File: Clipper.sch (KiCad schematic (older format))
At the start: 38 parts

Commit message: First complete system.  Still a few things to check.
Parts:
- removed C? (x3): C, ~, symbol C
- removed R? (x7): 4.7k, ~, symbol R
- added C? (x3): 470n, ~, symbol C
- added R? (x7): 1k, ~, symbol R
- C?: value C -> 470n; Type (none) -> Ceramic
- R?: value 4.7k -> 1k
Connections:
- net +15V: now also C?.1
- net -15V: now also C?.2, C?.2
- net AGND: now also C?.1, C?.1, C?.2
- net LIN: now also R?.1
- net RIN: now also R?.1
- net ROUT: now also R?.2
- net at D?.2 (K), R?.1: now also R?.1 (x4)
- net at R?.1, U?.6 (_): now also R?.2, R?.2, R?.2
- net at U?.6 (_): now also R?.1, R?.2, R?.2, R?.2
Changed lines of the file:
@@
 LIBS:my-conn
 LIBS:ADC-cache
-EELAYER 24 0
+EELAYER 27 0
 EELAYER END
 $Descr A4 11693 8268
@@
 Sheet 5 6
 Title ""
-Date "12 may 2014"
+Date "21 may 2014"
 Rev ""
 Comp ""
@@
 $Comp
 L R R?
-U 1 1 536E7363
-P 3600 3400
-F 0 "R?" V 3680 3400 40  0000 C CNN
-F 1 "4.7k" V 3607 3401 40  0000 C CNN
-F 2 "~" V 3530 3400 30  0000 C CNN
-F 3 "~" H 3600 3400 30  0000 C CNN
-	1    3600 3400
-	0    -1   -1   0
-$EndComp
-$Comp
-L R R?
-U 1 1 536E73C0
-P 3600 3700
-F 0 "R?" V 3680 3700 40  0000 C CNN
-F 1 "4.7k" V 3607 3701 40  0000 C CNN
-F 2 "~" V 3530 3700 30  0000 C CNN
-F 3 "~" H 3600 3700 30  0000 C CNN
-	1    3600 3700
-	0    -1   -1   0
-$EndComp
-$Comp
-L R R?
-U 1 1 536E742F
-P 3600 4000
-F 0 "R?" V 3680 4000 40  0000 C CNN
-F 1 "4.7k" V 3607 4001 40  0000 C CNN
-F 2 "~" V 3530 4000 30  0000 C CNN
-F 3 "~" H 3600 4000 30  0000 C CNN
-	1    3600 4000
-	0    -1   -1   0
-$EndComp
-$Comp
-L R R?
 U 1 1 536E799F
 P 1450 4950
@@
 P 4750 3200
 F 0 "R?" V 4830 3200 40  0000 C CNN
-F 1 "4.7k" V 4757 3201 40  0000 C CNN
+F 1 "1k" V 4757 3201 40  0000 C CNN
 F 2 "~" V 4680 3200 30  0000 C CNN
 F 3 "~" H 4750 3200 30  0000 C CNN
@@
 $Comp
 L R R?
-U 1 1 536E837F
-P 9000 3400
-F 0 "R?" V 9080 3400 40  0000 C CNN
-F 1 "4.7k" V 9007 3401 40  0000 C CNN
-F 2 "~" V 8930 3400 30  0000 C CNN
-F 3 "~" H 9000 3400 30  0000 C CNN
-	1    9000 3400
-	0    -1   -1   0
-$EndComp
-$Comp
-L R R?
-U 1 1 536E8385
-P 9000 3700
-F 0 "R?" V 9080 3700 40  0000 C CNN
-F 1 "4.7k" V 9007 3701 40  0000 C CNN
-F 2 "~" V 8930 3700 30  0000 C CNN
-F 3 "~" H 9000 3700 30  0000 C CNN
-	1    9000 3700
-	0    -1   -1   0
-$EndComp
-$Comp
-L R R?
-U 1 1 536E838B
-P 9000 4000
-F 0 "R?" V 9080 4000 40  0000 C CNN
-F 1 "4.7k" V 9007 4001 40  0000 C CNN
-F 2 "~" V 8930 4000 30  0000 C CNN
-F 3 "~" H 9000 4000 30  0000 C CNN
-	1    9000 4000
-	0    -1   -1   0
-$EndComp
-$Comp
-L R R?
 U 1 1 536E8391
 P 6850 4950
@@
 Text HLabel 9550 4000 3    60   Input ~ 0
 AGND
-$Comp
-L R R?
-U 1 1 536E83F0
-P 10150 3200
-F 0 "R?" V 10230 3200 40  0000 C CNN
-F 1 "4.7k" V 10157 3201 40  0000 C CNN
-F 2 "~" V 10080 3200 30  0000 C CNN
-F 3 "~" H 10150 3200 30  0000 C CNN
-	1    10150 3200
-	0    -1   -1   0
-$EndComp
 Text HLabel 10050 3400 0    60   Input ~ 0
 +15V
@@
 P 5450 1700
 F 0 "C?" H 5450 1800 40  0000 L CNN
-F 1 "C" H 5456 1615 40  0000 L CNN
+F 1 "470n" H 5456 1615 40  0000 L CNN
 F 2 "~" H 5488 1550 30  0000 C CNN
 F 3 "~" H 5450 1700 60  0000 C CNN
+F 4 "Ceramic" H 5450 1700 60  0001 C CNN "Type"
 	1    5450 1700
-	1    0    0    -1
-$EndComp
-$Comp
-L C C?
-U 1 1 536EC1ED
-P 5800 1700
-F 0 "C?" H 5800 1800 40  0000 L CNN
-F 1 "C" H 5806 1615 40  0000 L CNN
-F 2 "~" H 5838 1550 30  0000 C CNN
-F 3 "~" H 5800 1700 60  0000 C CNN
-	1    5800 1700
 	1    0    0    -1
 $EndComp
@@
 Text HLabel 5250 1900 0    60   Input ~ 0
 AGND
-$Comp
-L C C?
-U 1 1 536EC4B0
-P 5450 2100
-F 0 "C?" H 5450 2200 40  0000 L CNN
-F 1 "C" H 5456 2015 40  0000 L CNN
-F 2 "~" H 5488 1950 30  0000 C CNN
-F 3 "~" H 5450 2100 60  0000 C CNN
-	1    5450 2100
-	1    0    0    -1
-$EndComp
-$Comp
-L C C?
-U 1 1 536EC4B6
-P 5800 2100
-F 0 "C?" H 5800 2200 40  0000 L CNN
-F 1 "C" H 5806 2015 40  0000 L CNN
-F 2 "~" H 5838 1950 30  0000 C CNN
-F 3 "~" H 5800 2100 60  0000 C CNN
-	1    5800 2100
-	1    0    0    -1
-$EndComp
 Wire Wire Line
 	1850 2850 1850 3050
@@
 Wire Wire Line
 	5250 1900 5800 1900
+$Comp
+L C C?
+U 1 1 537C3D88
+P 5800 1700
+F 0 "C?" H 5800 1800 40  0000 L CNN
+F 1 "470n" H 5806 1615 40  0000 L CNN
+F 2 "~" H 5838 1550 30  0000 C CNN
+F 3 "~" H 5800 1700 60  0000 C CNN
+F 4 "Ceramic" H 5800 1700 60  0001 C CNN "Type"
+	1    5800 1700
+	1    0    0    -1
+$EndComp
+$Comp
+L C C?
+U 1 1 537C3D8F
+P 5450 2100
+F 0 "C?" H 5450 2200 40  0000 L CNN
+F 1 "470n" H 5456 2015 40  0000 L CNN
+F 2 "~" H 5488 1950 30  0000 C CNN
+F 3 "~" H 5450 2100 60  0000 C CNN
+F 4 "Ceramic" H 5450 2100 60  0001 C CNN "Type"
+	1    5450 2100
+	1    0    0    -1
+$EndComp
+$Comp
+L C C?
+U 1 1 537C3D96
+P 5800 2100
+F 0 "C?" H 5800 2200 40  0000 L CNN
+F 1 "470n" H 5806 2015 40  0000 L CNN
+F 2 "~" H 5838 1950 30  0000 C CNN
+F 3 "~" H 5800 2100 60  0000 C CNN
+F 4 "Ceramic" H 5800 2100 60  0001 C CNN "Type"
+	1    5800 2100
+	1    0    0    -1
+$EndComp
+$Comp
+L R R?
+U 1 1 537C500E
+P 3600 3400
+F 0 "R?" V 3680 3400 40  0000 C CNN
+F 1 "1k" V 3607 3401 40  0000 C CNN
+F 2 "~" V 3530 3400 30  0000 C CNN
+F 3 "~" H 3600 3400 30  0000 C CNN
+	1    3600 3400
+	0    -1   -1   0
+$EndComp
+$Comp
+L R R?
+U 1 1 537C5014
+P 3600 3700
+F 0 "R?" V 3680 3700 40  0000 C CNN
+F 1 "1k" V 3607 3701 40  0000 C CNN
+F 2 "~" V 3530 3700 30  0000 C CNN
+F 3 "~" H 3600 3700 30  0000 C CNN
+	1    3600 3700
+	0    -1   -1   0
+$EndComp
+$Comp
+L R R?
+U 1 1 537C501A
+P 3600 4000
+F 0 "R?" V 3680 4000 40  0000 C CNN
+F 1 "1k" V 3607 4001 40  0000 C CNN
+F 2 "~" V 3530 4000 30  0000 C CNN
+F 3 "~" H 3600 4000 30  0000 C CNN
+	1    3600 4000
+	0    -1   -1   0
+$EndComp
+$Comp
+L R R?
+U 1 1 537C5020
+P 9000 3400
+F 0 "R?" V 9080 3400 40  0000 C CNN
+F 1 "1k" V 9007 3401 40  0000 C CNN
+F 2 "~" V 8930 3400 30  0000 C CNN
+F 3 "~" H 9000 3400 30  0000 C CNN
+	1    9000 3400
+	0    -1   -1   0
+$EndComp
+$Comp
+L R R?
+U 1 1 537C5026
+P 9000 3700
+F 0 "R?" V 9080 3700 40  0000 C CNN
+F 1 "1k" V 9007 3701 40  0000 C CNN
+F 2 "~" V 8930 3700 30  0000 C CNN
+F 3 "~" H 9000 3700 30  0000 C CNN
+	1    9000 3700
+	0    -1   -1   0
+$EndComp
+$Comp
+L R R?
+U 1 1 537C502C
+P 9000 4000
+F 0 "R?" V 9080 4000 40  0000 C CNN
+F 1 "1k" V 9007 4001 40  0000 C CNN
+F 2 "~" V 8930 4000 30  0000 C CNN
+F 3 "~" H 9000 4000 30  0000 C CNN
+	1    9000 4000
+	0    -1   -1   0
+$EndComp
+$Comp
+L R R?
+U 1 1 537C5032
+P 10150 3200
+F 0 "R?" V 10230 3200 40  0000 C CNN
+F 1 "1k" V 10157 3201 40  0000 C CNN
+F 2 "~" V 10080 3200 30  0000 C CNN
+F 3 "~" H 10150 3200 30  0000 C CNN
+	1    10150 3200
+	0    -1   -1   0
+$EndComp
 $EndSCHEMATC

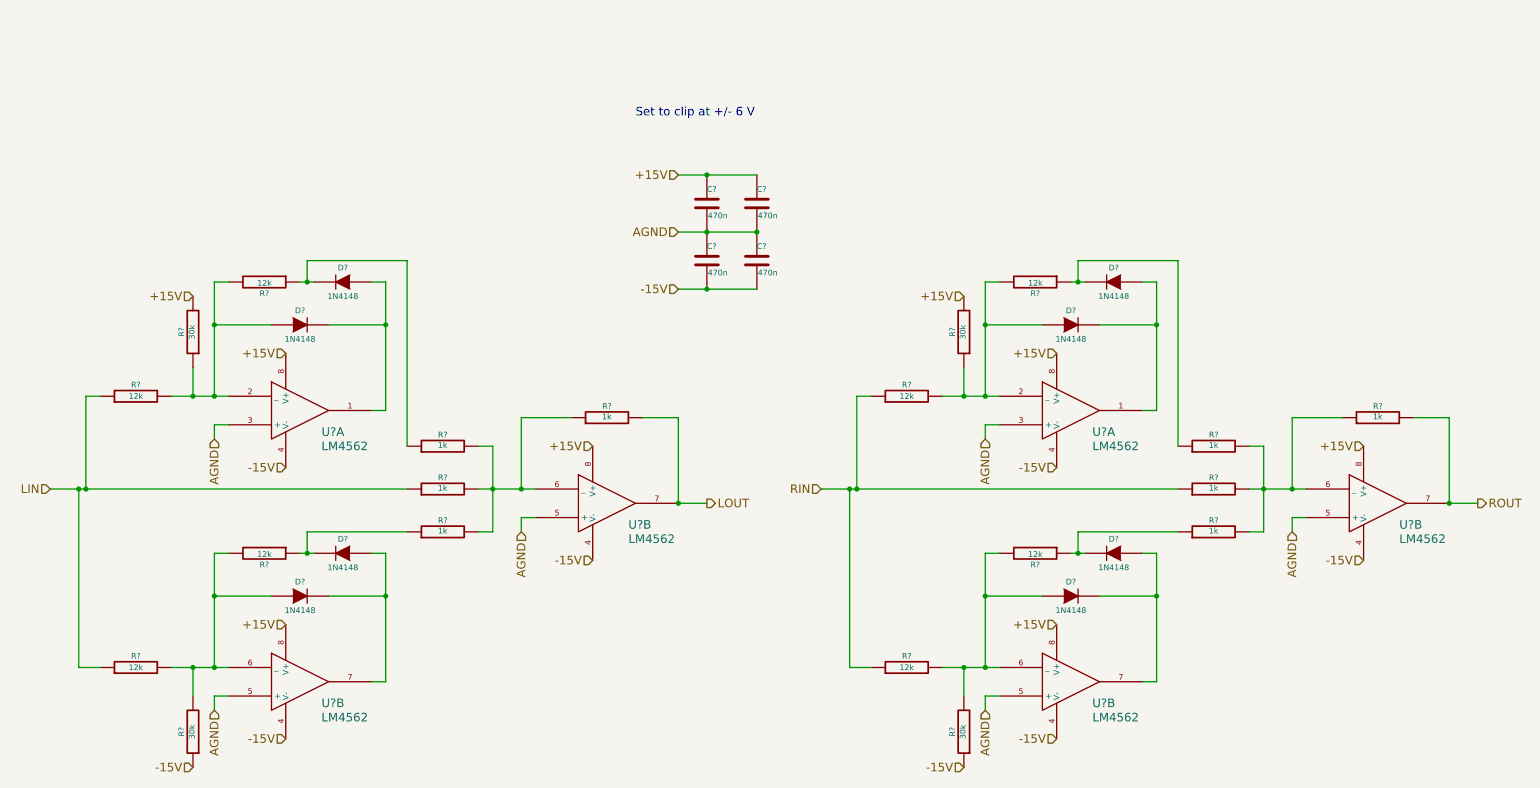
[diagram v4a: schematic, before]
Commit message: Noise analysis completed; signal section finished.
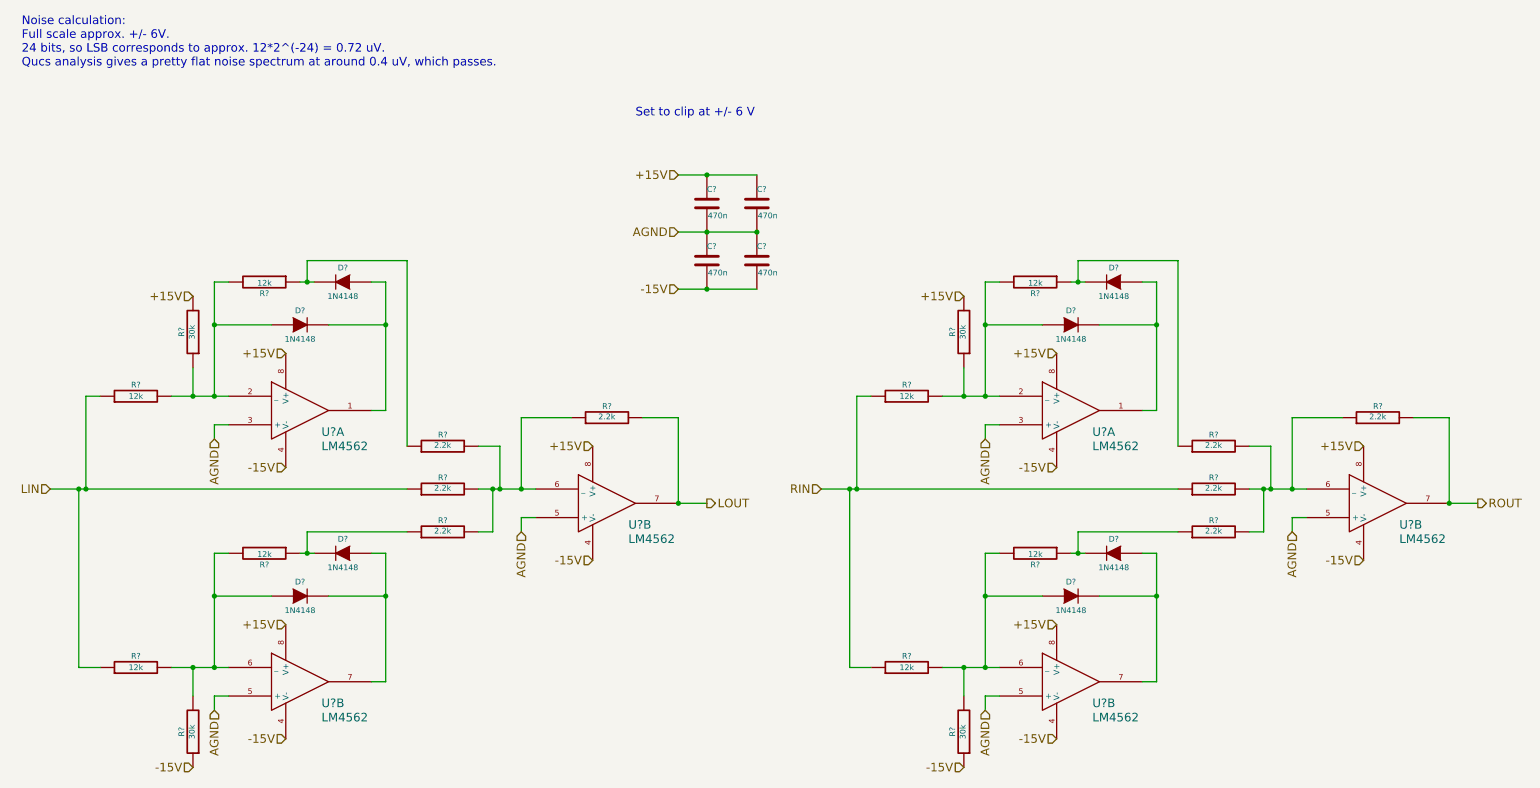
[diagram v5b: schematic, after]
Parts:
- removed R? (x7): 1k, ~, symbol R
- added R? (x7): 2.2k, ~, symbol R
- R?: value 1k -> 2.2k
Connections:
- net LIN: now also R?.1
- net LOUT: now also R?.2
- net RIN: now also R?.1
- net ROUT: now also R?.2
- net at D?.2 (K), R?.1: now also R?.1 (x3)
- net at R?.2, U?.6 (_): now also R?.1, R?.2, R?.2
- net at U?.6 (_): now also R?.1, R?.2, R?.2, R?.2
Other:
- note added: "Noise calculation:\nFull scale approx. +/- 6V.\n24 bits, so LSB corresponds to approx. 12*2^(-24) = 0.72 uV.\nQucs analysis gives a pretty flat noise spectrum at around 0.4 uV, which passes."
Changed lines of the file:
@@
 Text HLabel 4150 4000 3    60   Input ~ 0
 AGND
-$Comp
-L R R?
-U 1 1 536E7BF7
-P 4750 3200
-F 0 "R?" V 4830 3200 40  0000 C CNN
-F 1 "1k" V 4757 3201 40  0000 C CNN
-F 2 "~" V 4680 3200 30  0000 C CNN
-F 3 "~" H 4750 3200 30  0000 C CNN
-	1    4750 3200
-	0    -1   -1   0
-$EndComp
 Text HLabel 4650 3400 0    60   Input ~ 0
 +15V
@@
 	3350 2100 2650 2100
 Wire Wire Line
-	3850 3400 3950 3400
-Wire Wire Line
-	3950 3400 3950 4000
+	3850 3400 4000 3400
 Connection ~ 1100 3700
 Wire Wire Line
@@
 	8750 2100 8050 2100
 Wire Wire Line
-	9250 3400 9350 3400
-Wire Wire Line
-	9350 3400 9350 4000
+	9250 3400 9400 3400
 Connection ~ 6500 3700
 Wire Wire Line
@@
 P 3600 3400
 F 0 "R?" V 3680 3400 40  0000 C CNN
-F 1 "1k" V 3607 3401 40  0000 C CNN
+F 1 "2.2k" V 3607 3401 40  0000 C CNN
 F 2 "~" V 3530 3400 30  0000 C CNN
 F 3 "~" H 3600 3400 30  0000 C CNN
@@
 	0    -1   -1   0
 $EndComp
-$Comp
-L R R?
-U 1 1 537C5014
+Wire Wire Line
+	4000 3400 4000 3700
+Connection ~ 4000 3700
+Wire Wire Line
+	3950 3700 3950 4000
+Wire Wire Line
+	9400 3400 9400 3700
+Connection ~ 9400 3700
+Wire Wire Line
+	9350 3700 9350 4000
+Text Notes 650  750  0    60   ~ 0
+Noise calculation:\nFull scale approx. +/- 6V.\n24 bits, so LSB corresponds to approx. 12*2^(-24) = 0.72 uV.\nQucs analysis gives a pretty flat noise spectrum at around 0.4 uV, which passes.
+$Comp
+L R R?
+U 1 1 537CA2E9
 P 3600 3700
 F 0 "R?" V 3680 3700 40  0000 C CNN
-F 1 "1k" V 3607 3701 40  0000 C CNN
+F 1 "2.2k" V 3607 3701 40  0000 C CNN
 F 2 "~" V 3530 3700 30  0000 C CNN
 F 3 "~" H 3600 3700 30  0000 C CNN
@@
 $Comp
 L R R?
-U 1 1 537C501A
+U 1 1 537CA2EF
 P 3600 4000
 F 0 "R?" V 3680 4000 40  0000 C CNN
-F 1 "1k" V 3607 4001 40  0000 C CNN
+F 1 "2.2k" V 3607 4001 40  0000 C CNN
 F 2 "~" V 3530 4000 30  0000 C CNN
 F 3 "~" H 3600 4000 30  0000 C CNN
@@
 $Comp
 L R R?
-U 1 1 537C5020
+U 1 1 537CA2F5
+P 4750 3200
+F 0 "R?" V 4830 3200 40  0000 C CNN
+F 1 "2.2k" V 4757 3201 40  0000 C CNN
+F 2 "~" V 4680 3200 30  0000 C CNN
+F 3 "~" H 4750 3200 30  0000 C CNN
+	1    4750 3200
+	0    -1   -1   0
+$EndComp
+$Comp
+L R R?
+U 1 1 537CA2FB
 P 9000 3400
 F 0 "R?" V 9080 3400 40  0000 C CNN
-F 1 "1k" V 9007 3401 40  0000 C CNN
+F 1 "2.2k" V 9007 3401 40  0000 C CNN
 F 2 "~" V 8930 3400 30  0000 C CNN
 F 3 "~" H 9000 3400 30  0000 C CNN
@@
 $Comp
 L R R?
-U 1 1 537C5026
+U 1 1 537CA301
 P 9000 3700
 F 0 "R?" V 9080 3700 40  0000 C CNN
-F 1 "1k" V 9007 3701 40  0000 C CNN
+F 1 "2.2k" V 9007 3701 40  0000 C CNN
 F 2 "~" V 8930 3700 30  0000 C CNN
 F 3 "~" H 9000 3700 30  0000 C CNN
@@
 $Comp
 L R R?
-U 1 1 537C502C
+U 1 1 537CA307
 P 9000 4000
 F 0 "R?" V 9080 4000 40  0000 C CNN
-F 1 "1k" V 9007 4001 40  0000 C CNN
+F 1 "2.2k" V 9007 4001 40  0000 C CNN
 F 2 "~" V 8930 4000 30  0000 C CNN
 F 3 "~" H 9000 4000 30  0000 C CNN
@@
 $Comp
 L R R?
-U 1 1 537C5032
+U 1 1 537CA30D
 P 10150 3200
 F 0 "R?" V 10230 3200 40  0000 C CNN
-F 1 "1k" V 10157 3201 40  0000 C CNN
+F 1 "2.2k" V 10157 3201 40  0000 C CNN
 F 2 "~" V 10080 3200 30  0000 C CNN
 F 3 "~" H 10150 3200 30  0000 C CNN
